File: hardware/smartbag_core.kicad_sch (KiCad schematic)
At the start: 111 parts, among them J1 FFC optics, 12 way, J2 LiPo 3.7V 2000mAh + NTC, J3 Qi RX coil, J4 FFC FSR matrix, 24 way, J5 SWD debug, Q1 SI2302CDS-T1-GE3, U1 nRF54L15-QFAA-R, U11 BQ51013BRHLR, U2 Acconeer A121, U3 nPM1300-QEAA-R7, U4 BMI270, U5 DRV5032FBDBZR, U6 Acconeer A121, U7 CD74HC4067SM96, U8 TLV9064IPWR, U9 TLV9064IPWR, Y1 32 MHz Cl=8pF, Y2 24 MHz, Y3 24 MHz, Y4 32.768 kHz Cl=9pF

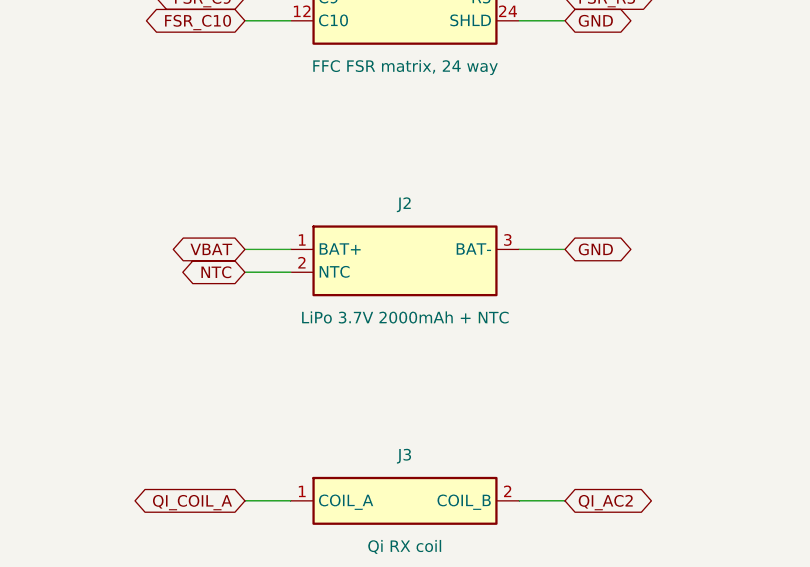
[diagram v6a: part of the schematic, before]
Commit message: set -e was decoration: every step was piped to tail
A crash inside specctra.py printed its traceback and the pipeline carried
straight on into fill, stitch and route. The board came out with 117
unconnected pads out of an import that had never happened, and reported
it as a normal run.

The cause is one line per script: `python3 ... | tail -1`. A pipeline's
exit status is the LAST command's, tail always succeeds, and `set -e`
therefore never saw anything fail. Five scripts now set pipefail.

⛔ AND THE CRASH ITSELF WAS TWO CLEANUP PASSES ON ONE BOARD. pcbnew's
GetTracks() is a live wrapper: once anything has been removed, it comes
back as a raw SWIG pointer that will not iterate — and on this machine
the second pass segfaulted rather than raising. Both cleanups now decide
against ONE snapshot and the caller removes once. That is not tidiness,
it is the only order that works.

The new cleanup is worth having on its own. Freerouting's optimiser
splits polylines and rounds the joins, leaving segments 0.0001 mm long —
a tenth of a micron — sitting at corners. Nine clearance violations on an
otherwise clean board were pairs of (a real track, one of those), because
a sliver still carries a full track width and so still has a clearance
envelope, pointing wherever the rounding chose.

⚠️ The threshold is 5 um and the number that justifies it is the track
WIDTH, not the fabricator's resolution: the narrowest track here is
100 um, so a 5 um segment lies entirely inside the copper it joins at
either end, twenty times over. Removing it cannot disconnect anything.
The first attempt used 1 um and left a 1.6 um stub behind, which DRC then
reported like any other track.

maze.py can now rip up as well as add. A board that came back with two
tracks 0.127 mm apart where the Power class asks for 0.15 was one it had
nothing to say about — it could only add copper, so it refused its own
routes for making a bad number worse and stopped. It now deletes the
shorter track of each clearance p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
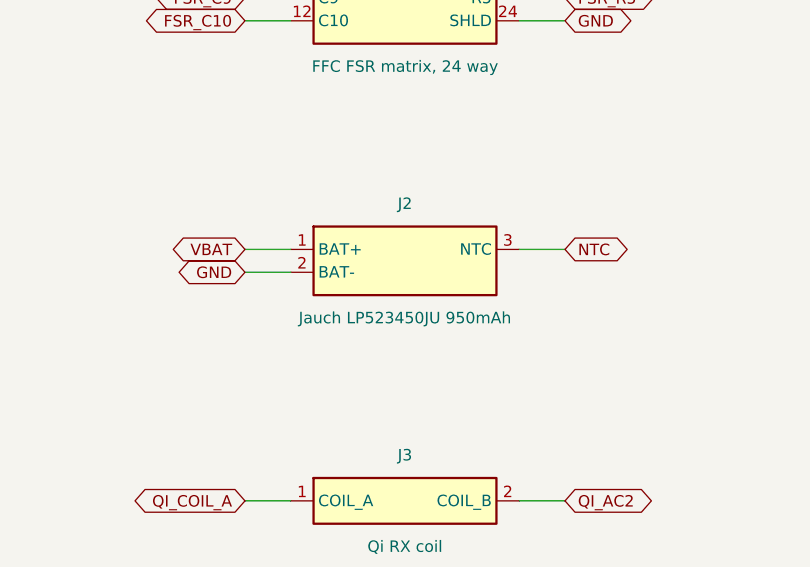
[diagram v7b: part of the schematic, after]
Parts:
- J2: value LiPo 3.7V 2000mAh + NTC -> Jauch LP523450JU 950mAh; footprint Connector_JST:JST_SH_SM03B-SRSS-TB_1x03-1MP_P1.00mm_Horizontal -> Connector_JST:JST_PH_S3B-PH-K_1x03_P2.00mm_Horizontal
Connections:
- net GND: now also J2.2 (BAT-); no longer J2.3 (BAT-)
- net NTC: now also J2.3 (NTC); no longer J2.2 (NTC)
